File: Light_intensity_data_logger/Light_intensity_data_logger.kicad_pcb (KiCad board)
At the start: 2 copper layers, 105 x 69 mm, 28 parts, among them J1 Wire_to_Vbat, Q1 NTJD4001NT1G, Q2 NTJD4001NT1G, U1 BME280, U2 TCS34725FN, U3 TSL25911FN, U4 Teensy3.6

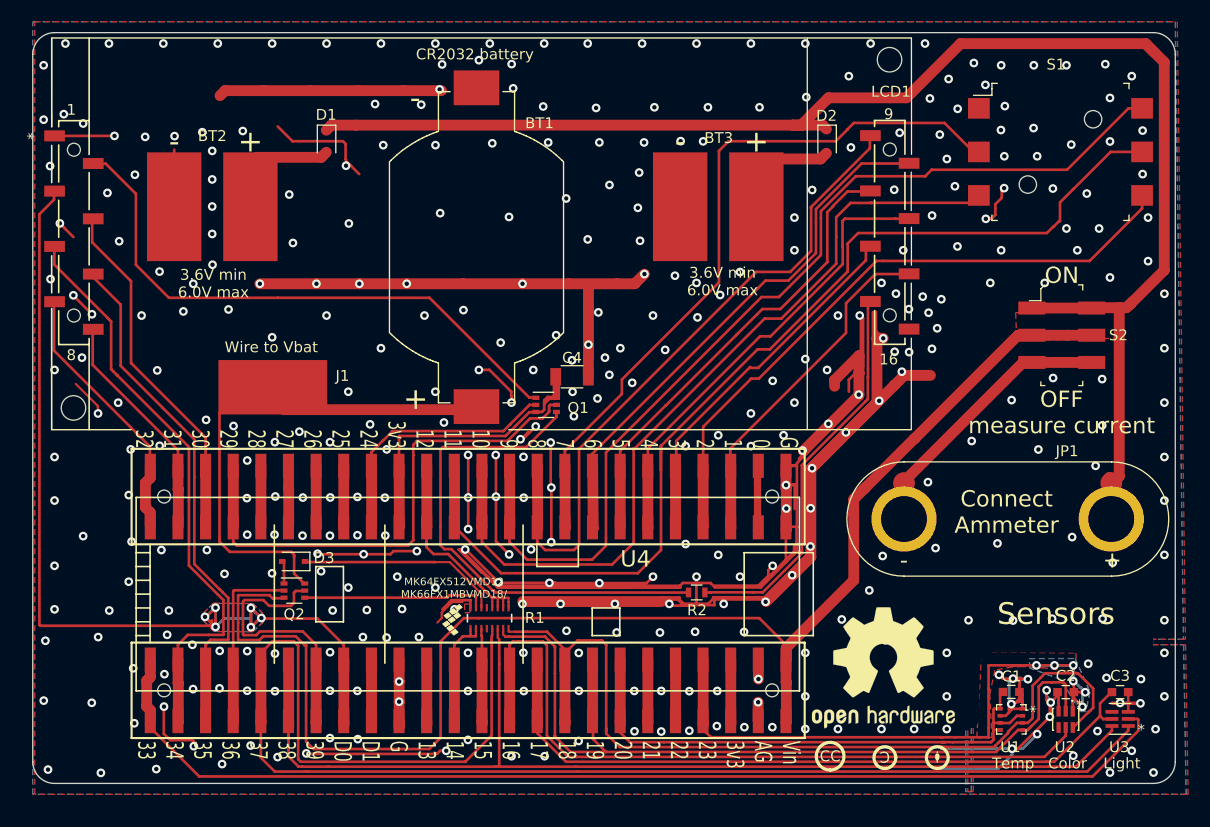
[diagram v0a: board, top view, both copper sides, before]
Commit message: PCBWay compatible - max PCB dim <100mm
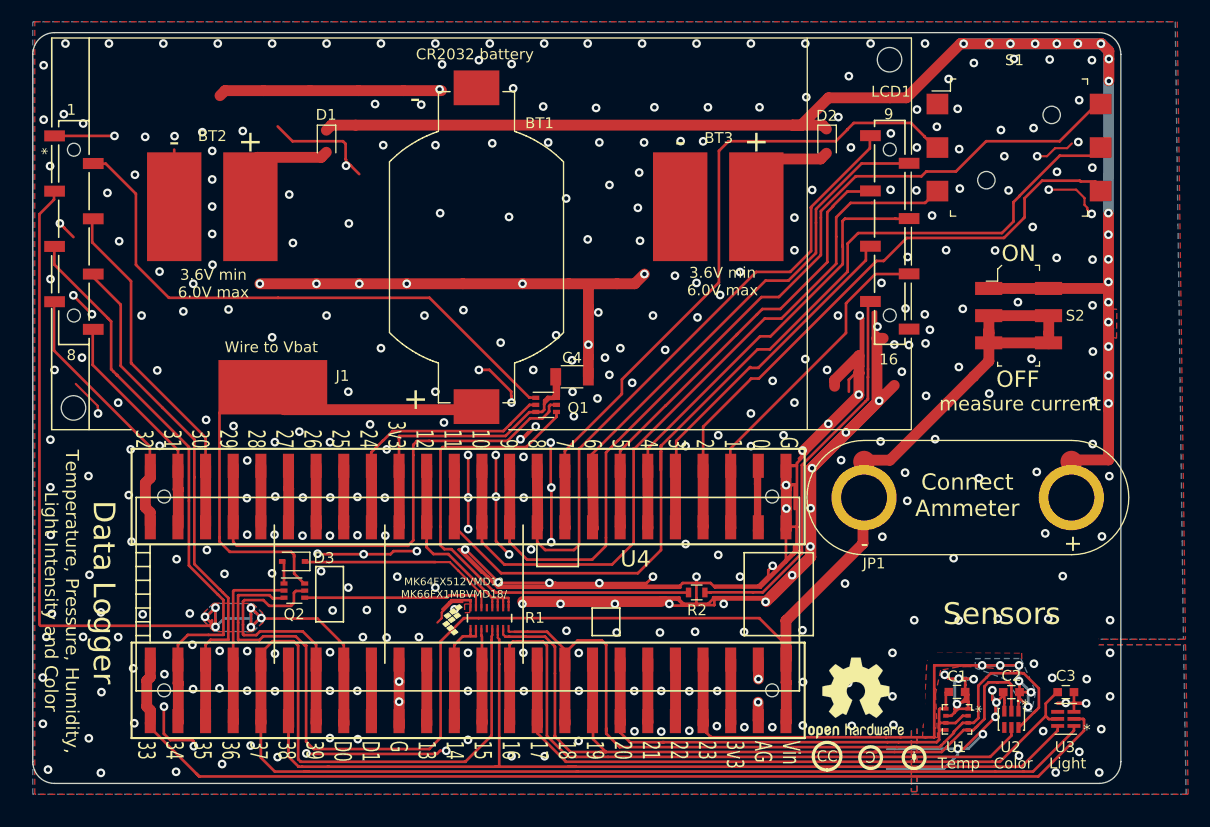
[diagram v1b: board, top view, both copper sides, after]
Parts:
- removed the REF*** at (151.2, 90.4)
- added REF***: OSHW-Logo2_9.8x8mm_SilkScreen, Symbols:OSHW-Logo2_9.8x8mm_SilkScreen, F.Cu at (148.7, 93.1)
- moved C1 4.99 mm to (157.9, 92.6)
- moved C2 4.99 mm to (162.9, 92.6)
- moved C3 4.99 mm to (167.9, 92.6)
- moved REF** 4.99 mm to (153.0, 87.0)
- moved U1 4.99 mm to (157.9, 95.1)
- moved U2 4.99 mm to (162.9, 95.1)
- moved U3 4.99 mm to (167.9, 95.1)
- moved S2 4.36 mm to (163.6, 58.0)
- moved JP1 4.17 mm to (149.4, 74.7)
- moved S1 3.83 mm to (163.6, 42.6)
- moved REF** 2.13 mm to (154.0, 98.6)
- moved REF** 1.31 mm to (150.0, 98.6)
- moved REF** 0.28 mm to (146.0, 98.5)
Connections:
- JP1 pad 1: Net-(JP1-Pad1) -> /Vin
- S2 pad 3: Net-(JP1-Pad1) -> /Vin
- S2 pad 6: Net-(JP1-Pad1) -> /Vin
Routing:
- net Net-(D1-Pad1): track 145.6 -> 177.7 mm, vias 0 -> 18
- net Net-(JP1-Pad1): track 28.6 -> 0.00 mm
- net /Vin: track 132.4 -> 157.7 mm
- net /SDA0: track 81.5 -> 76.1 mm
- net /Temp_Vcc: track 50.7 -> 45.6 mm
- net /Color_Vcc: track 62.7 -> 57.6 mm
- net /16*: track 71.0 -> 66.0 mm
- net /SCL1: track 136.6 -> 131.7 mm
- net /Light_Vcc: track 66.1 -> 61.2 mm
- net /33*: track 102.9 -> 98.3 mm
- net /SDA1: track 101.5 -> 97.2 mm
- net /SCL0: track 77.0 -> 72.7 mm
- net /10*: track 75.6 -> 71.7 mm
- net /7*: track 66.5 -> 62.6 mm
- net /11*: track 97.4 -> 93.6 mm
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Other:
- board size 105 x 69 mm -> 100 x 69 mm
- board text added: "Data Logger"
- board text added: "OFF"
- board text added: "Temperature, Pressure, Humidity, Light Intensity and Color"
- board text added: "measure current"
- board text removed: "OFF measure current"

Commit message: Fixed MOSFET issue - improved routing
Changed LCD to 4-pin only to free up pins
Routed data lines in clusters to leave open contiguous blocks of pins
Kept DAC0 line above PCB
Attached light interrupt to pin 21 - valid hibernate digital line
Used analog switch to pulse Vbat to DAC,
Put N-mos on GND side of LED.
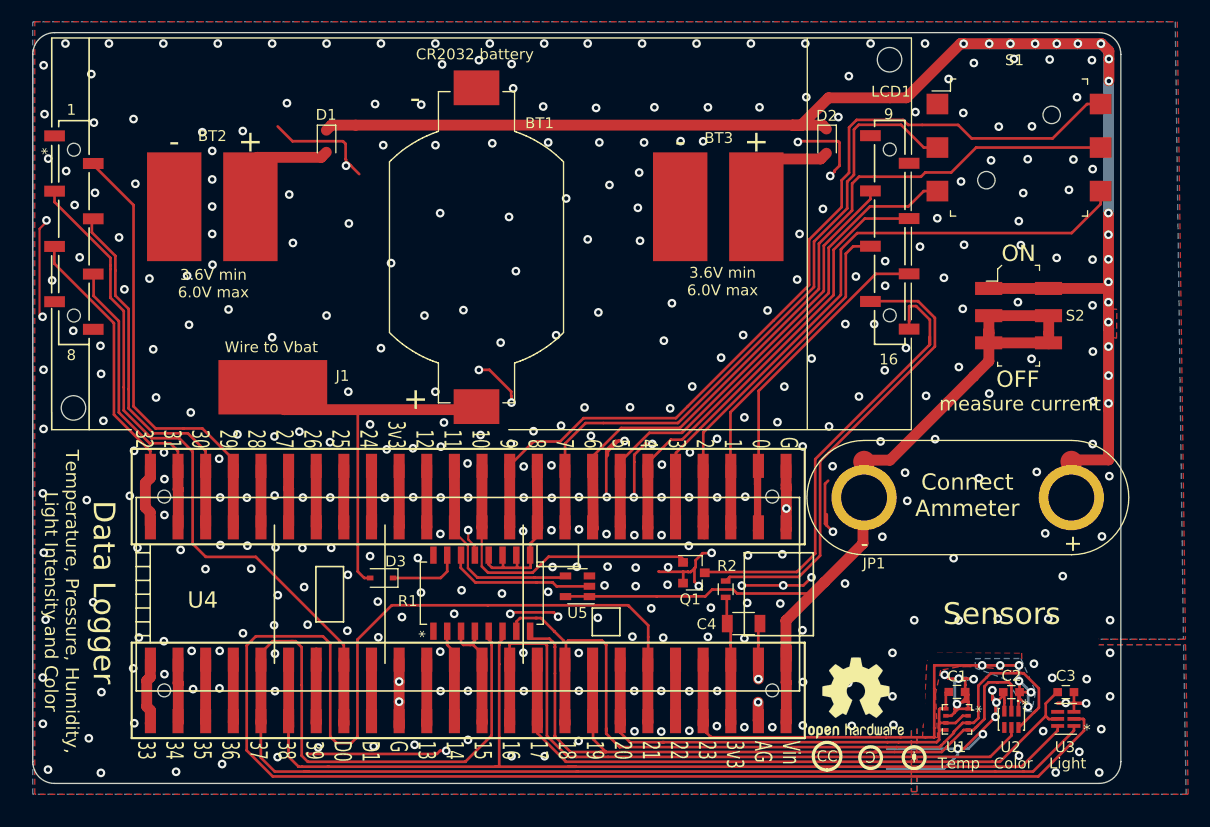
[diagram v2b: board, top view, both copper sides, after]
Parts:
- removed Q2: NTJD4001NT1G, TO_SOT_Packages_SMD:SOT-363_SC-70-6
- added U5: TS12A4514DBVR, TO_SOT_Packages_SMD:SOT-23-5, F.Cu at (123.1, 82.9)
- Q1: value NTJD4001NT1G -> Q_NMOS_GSD; footprint TO_SOT_Packages_SMD:SOT-363_SC-70-6 -> TO_SOT_Packages_SMD:SOT-23
- R1: footprint Ben_Custom:Resistor_array_1506_8x -> Ben_Custom:4816P-1-472LF
- moved C4 27.6 mm to (138.3, 86.3)
- moved Q1 20.6 mm to (133.8, 81.6)
- moved D3 8.23 mm to (105.1, 82.1)
- moved R2 2.68 mm to (136.7, 83.2), turned to 90 degrees
- moved R1 2.40 mm to (114.3, 83.5)
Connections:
- D3 pad 2: Net-(D3-Pad2) -> Net-(BT1-Pad+)
- LCD1 pad 10: /DB3 -> Net-(LCD1-Pad10)
- LCD1 pad 16: GND -> Net-(LCD1-Pad16)
- LCD1 pad 2: Net-(LCD1-Pad2) -> /LCD_Vcc
- LCD1 pad 7: /DB0 -> Net-(LCD1-Pad7)
- LCD1 pad 8: /DB1 -> Net-(LCD1-Pad8)
- LCD1 pad 9: /DB2 -> Net-(LCD1-Pad9)
- Q1 pad 1: Net-(LCD1-Pad2) -> /LED_PWM
- Q1 pad 2: /LCD_toggle -> GND
- Q1 pad 3: /3v3 -> Net-(LCD1-Pad16)
- R1 pad 1: /A0 -> Net-(R1-Pad1)
- R1 pad 13: Net-(R1-Pad13) -> GND
- R1 pad 14: Net-(D3-Pad1) -> Net-(R1-Pad14)
- R1 pad 15: Net-(Q2-Pad4) -> Net-(D3-Pad1)
- R1 pad 16: GND -> Net-(R1-Pad16)
- R1 pad 4: Net-(R1-Pad4) -> /A1
- R1 pad 7: /SCL0 -> /SDA0
- R1 pad 8: /SDA0 -> /SCL0
- R2 pad 1: Net-(Q1-Pad4) -> /3v3
- S1 pad 3: /10* -> /4*
- S1 pad 5: /11* -> /6*
- U3 pad 2: /33* -> /21*
- U4 pad 10: /DB2 -> /I2C_Pullup
- U4 pad 12: /10* -> /LED_PWM
- U4 pad 13: /11* -> /Bat_test
- U4 pad 14: /I2C_Pullup -> Net-(U4-Pad14)
- U4 pad 15: /3v3 -> Net-(U4-Pad15)
- U4 pad 16: /LCD_toggle -> Net-(U4-Pad16)
- U4 pad 2: Net-(U4-Pad2) -> /DB7
- U4 pad 21: /LED_PWM -> /LCD_Vcc
- U4 pad 23: /DB1 -> /E
- U4 pad 24: /DB0 -> /RW
- U4 pad 3: /DB7 -> /DB6
- U4 pad 30: /33* -> Net-(U4-Pad30)
- U4 pad 31: /RW -> Net-(U4-Pad31)
- U4 pad 32: /E -> Net-(U4-Pad32)
- U4 pad 33: /Coin_test -> Net-(U4-Pad33)
- U4 pad 36: /Bat_test -> Net-(U4-Pad36)
- U4 pad 48: Net-(U4-Pad48) -> /21*
- U4 pad 5: /DB6 -> /DB5
- U4 pad 51: Net-(U4-Pad51) -> /3v3
- U4 pad 6: /DB5 -> /4*
- U4 pad 8: /DB3 -> /6*
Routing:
- net GND: track 503.9 -> 168.2 mm, vias 390 -> 377
- net /21*: track 0.00 -> 159.5 mm
- net /33*: track 98.3 -> 0.00 mm
- net /11*: track 93.6 -> 0.00 mm
- net /10*: track 71.7 -> 0.00 mm
- net /6*: track 0.00 -> 69.5 mm
- net /DB2: track 62.2 -> 0.00 mm
- net /Vin: track 157.7 -> 102.3 mm
- net Net-(LCD1-Pad2): track 53.5 -> 0.00 mm
- net /DB3: track 49.7 -> 0.00 mm
- net /4*: track 0.00 -> 46.9 mm
- net Net-(Q1-Pad4): track 45.8 -> 0.00 mm
- net Net-(LCD1-Pad16): track 0.00 -> 42.5 mm
- net /LCD_Vcc: track 0.00 -> 41.3 mm
- net /LCD_contrast: track 93.8 -> 64.7 mm, vias 6 -> 0
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- removed copper zone on B.Cu, net /LCD_contrast
- removed copper zone on F.Cu, net /LCD_contrast

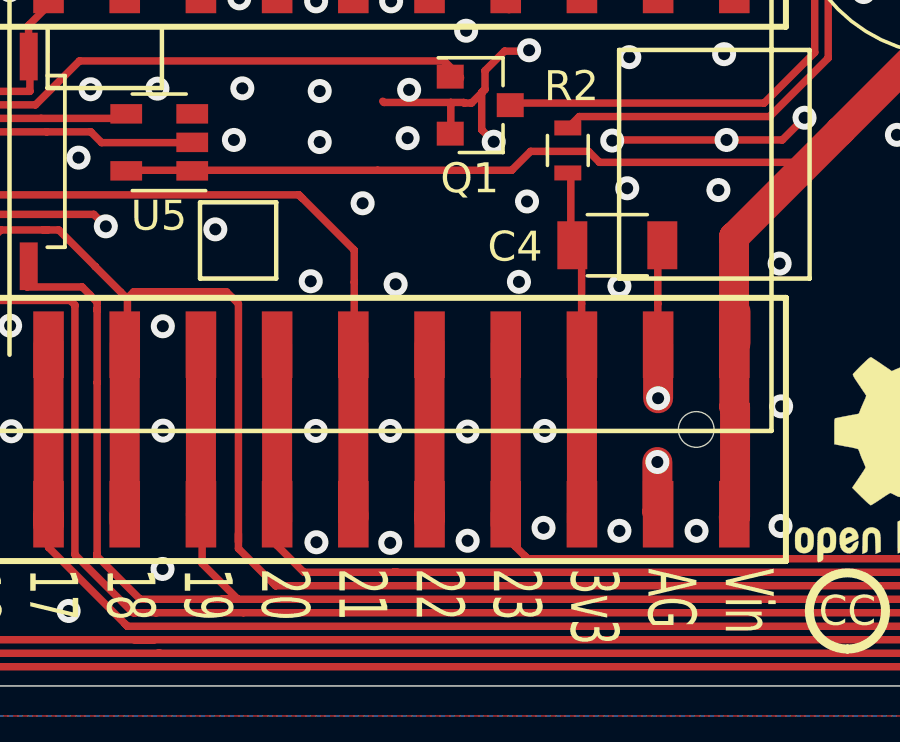
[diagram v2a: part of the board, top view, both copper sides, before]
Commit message: Add trace resistor between 3v3 and backlight cap for RC filtering
Trace resistor is 0.181 ohm
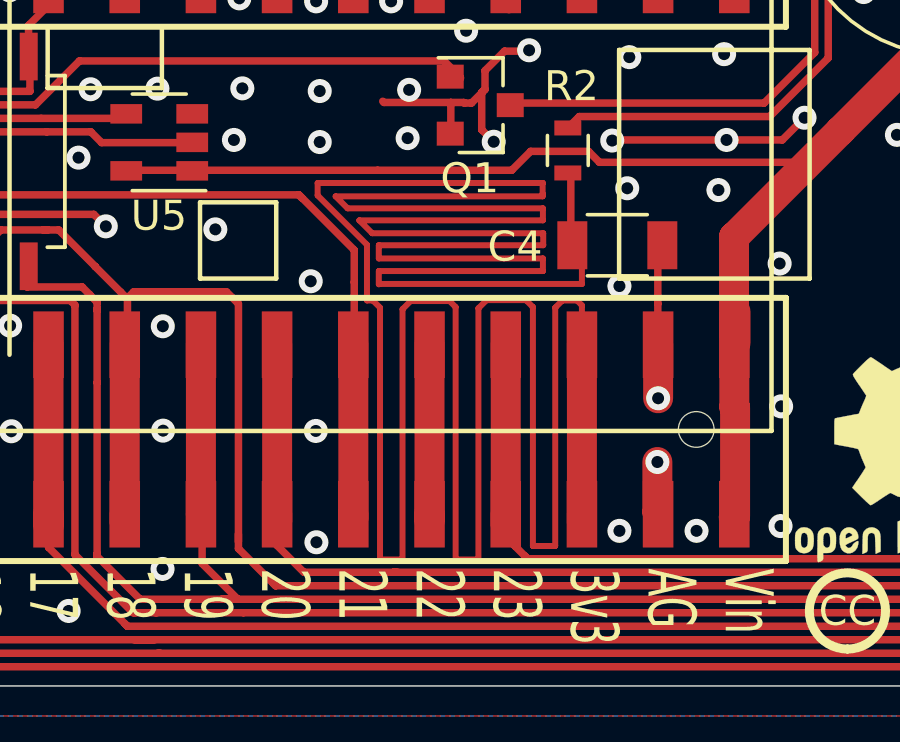
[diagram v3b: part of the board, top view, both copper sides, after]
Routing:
- net /3v3: track 12.2 -> 133.9 mm
- net GND: vias 377 -> 367

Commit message: This is draft of PCB submitted to PCBWay, logging works!!!
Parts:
- moved REF** 0.22 mm to (153.0, 87.2)
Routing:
- net GND: track 168.2 -> 167.9 mm, vias 367 -> 366

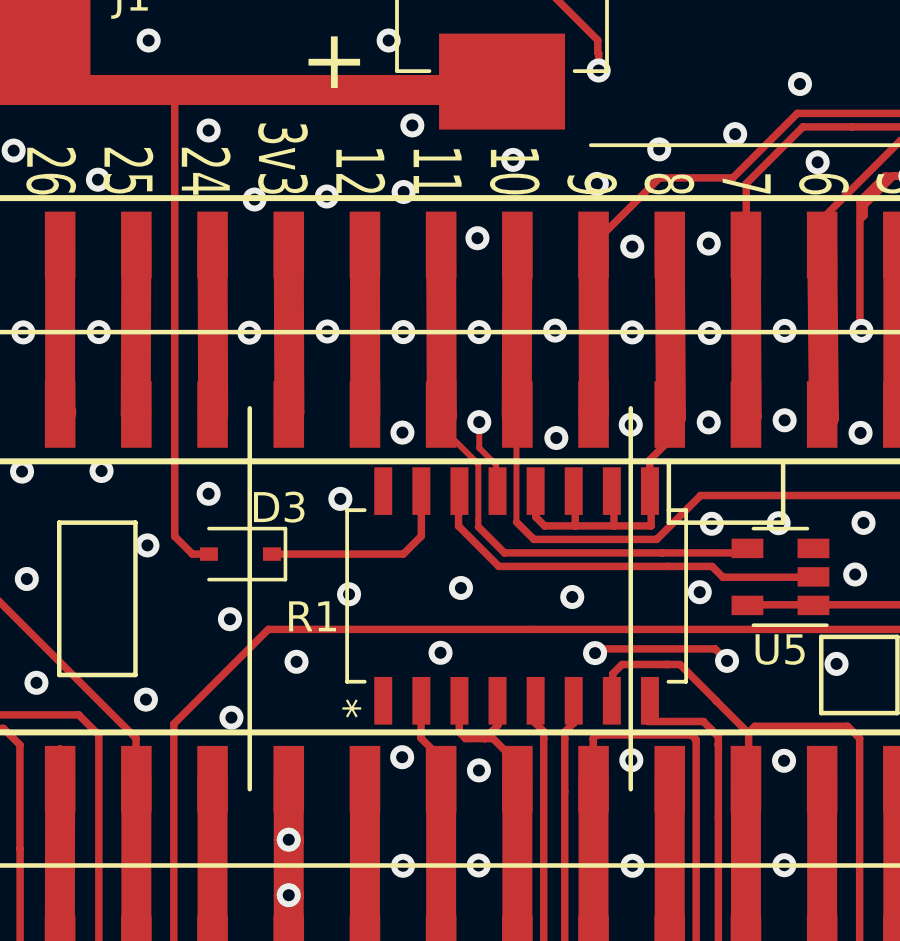
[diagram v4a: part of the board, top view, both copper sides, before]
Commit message: Add pulldown resistor to LCD LED PWM pin
Add pull down resistor so that the LCD LED with default to off if the pin is in a high impedance state.
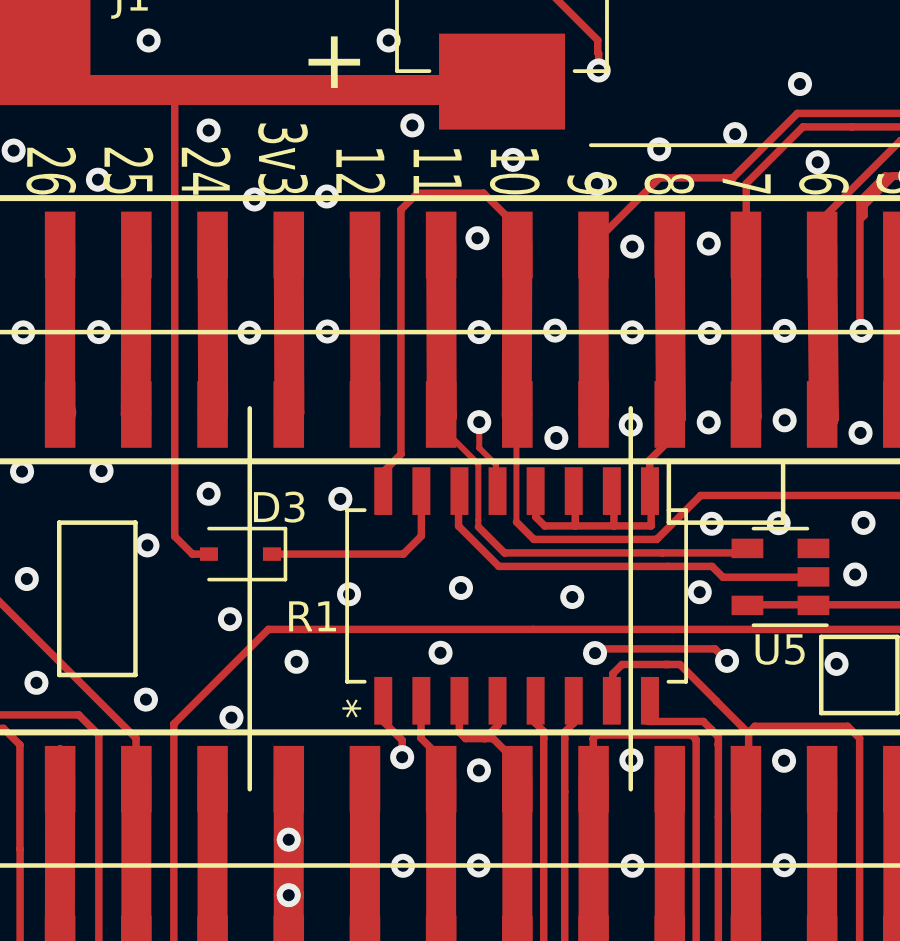
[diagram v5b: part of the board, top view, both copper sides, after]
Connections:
- R1 pad 1: Net-(R1-Pad1) -> GND
- R1 pad 16: Net-(R1-Pad16) -> /LED_PWM
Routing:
- net /LED_PWM: track 29.3 -> 44.1 mm
- net GND: track 167.9 -> 170.1 mm, vias 366 -> 363

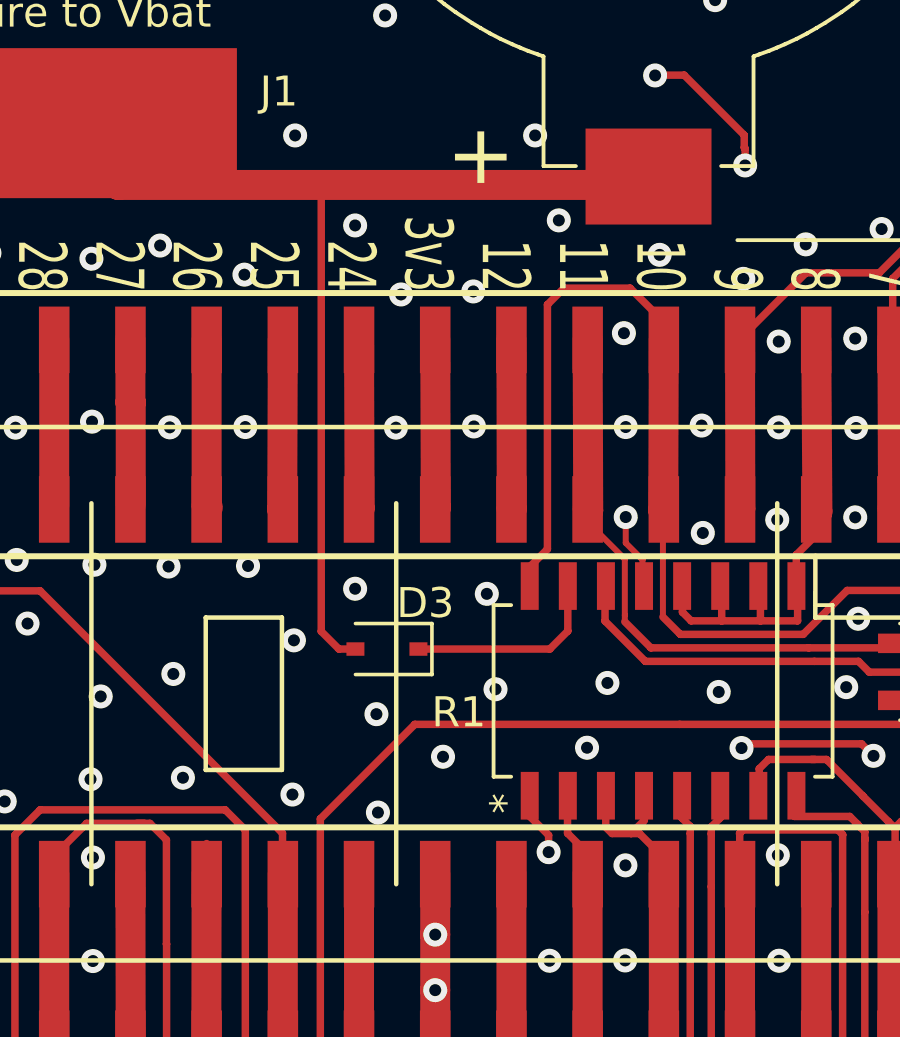
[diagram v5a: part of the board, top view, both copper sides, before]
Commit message: Remove Vbat check circuit
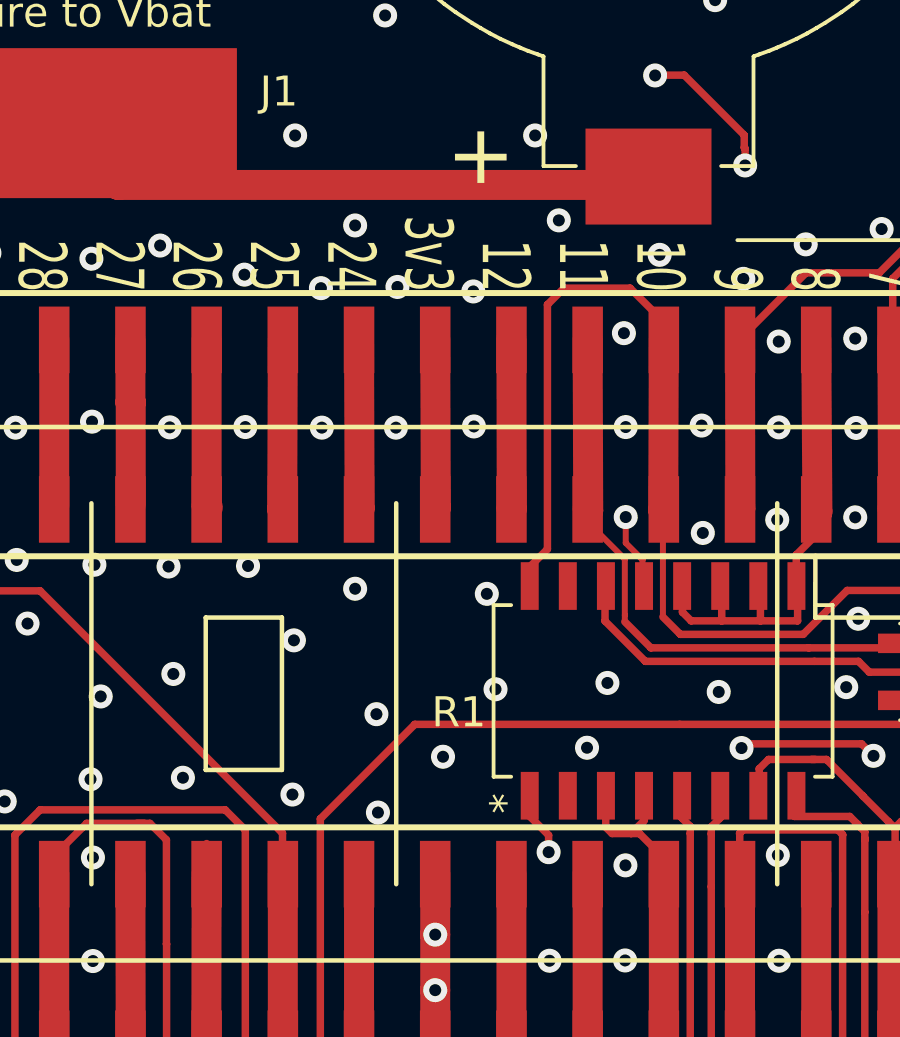
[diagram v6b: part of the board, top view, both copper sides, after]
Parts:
- removed D3: D, Diodes_SMD:D_SOD-323
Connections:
- R1 pad 2: /A0 -> Net-(R1-Pad2)
- U4 pad 41: /A0 -> Net-(U4-Pad41)
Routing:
- net Net-(BT1-Pad+): track 38.4 -> 22.0 mm
- net /A0: track 9.65 -> 0.00 mm
- net Net-(U4-Pad41): track 0.00 -> 7.47 mm
- net Net-(R1-Pad15): track 6.76 -> 0.00 mm
- net GND: vias 363 -> 365
